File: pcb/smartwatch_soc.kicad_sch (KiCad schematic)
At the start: 51 parts, among them J2 USB_B_Micro, Q1 PN2222A, Q2 PN2222A, Q3 BC338, Q4 BC338, SW1 EN_Switch, SW2 Button, SW3 Button, SW4 Button, SW5 Button, SW6 SW_MEC_5G, SW7 SW_MEC_5G, U1 ESP32-S3-MINI-1U, U2 LSM6DS3, U3 OLED_Display, U4 CP2102N-Axx-xQFN28

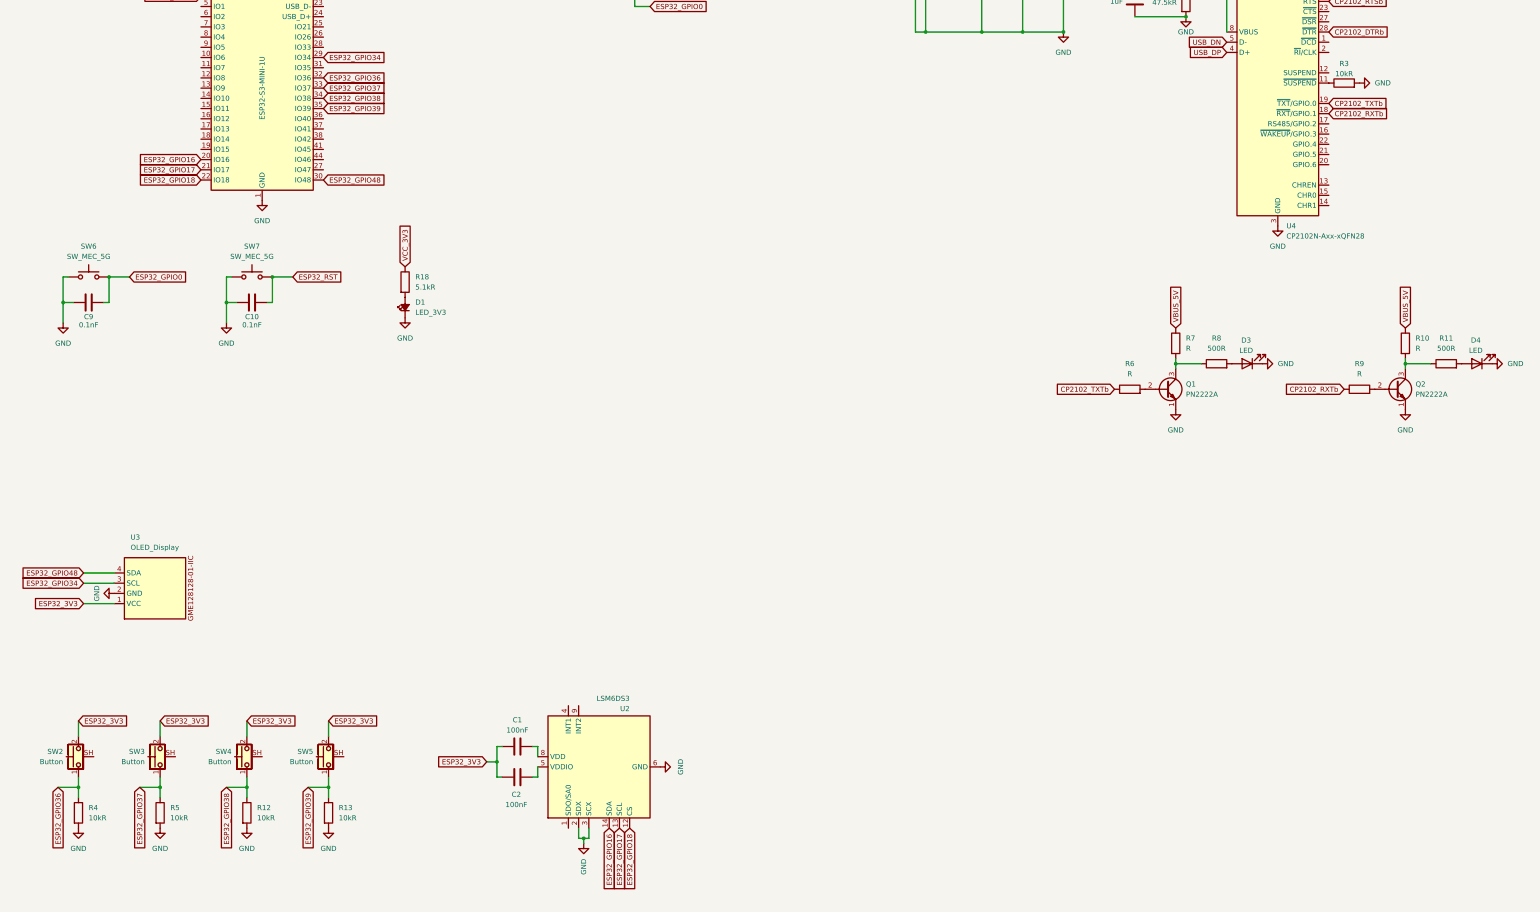
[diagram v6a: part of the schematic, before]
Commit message: fixed resistors for leds and capacitors for accelerometer
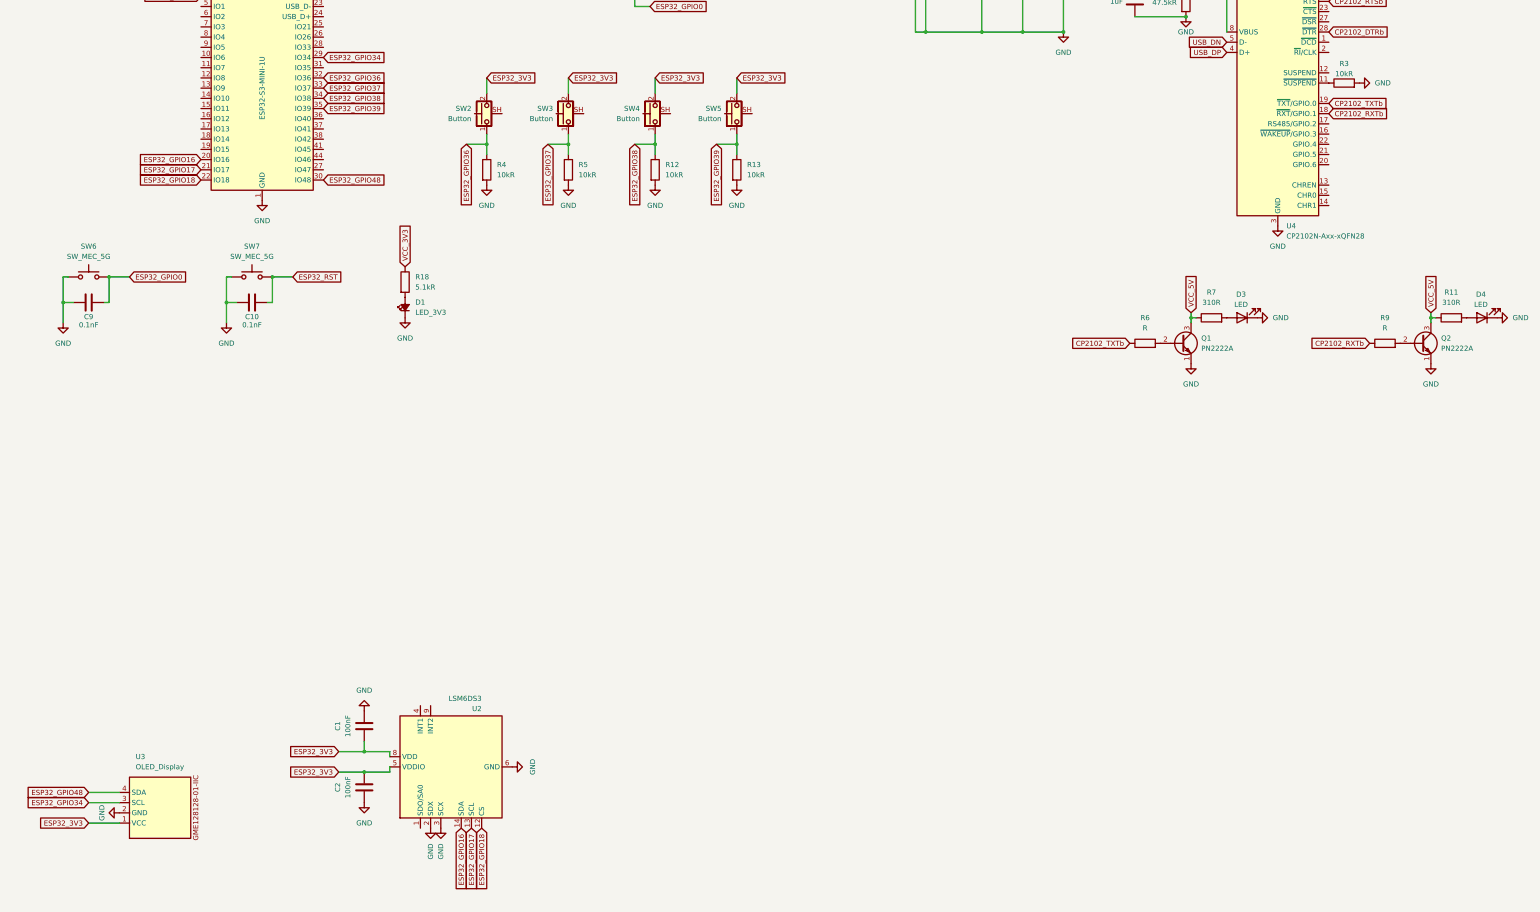
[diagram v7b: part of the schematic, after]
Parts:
- removed R10: R, Resistor_THT:R_Axial_DIN0204_L3.6mm_D1.6mm_P2.54mm_Vertical, symbol Device:R
- removed R8: 500R, Resistor_THT:R_Axial_DIN0204_L3.6mm_D1.6mm_P2.54mm_Vertical, symbol Device:R
- R11: value 500R -> 310R
- R7: value R -> 310R
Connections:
- net VBUS_5V is gone; now on net VCC_5V: R7.1
- net ESP32_3V3: now also C2.2, U2.5 (VDDIO), U2.8 (VDD); no longer C2.1
- net GND: now also C1.2, C2.1
- net VCC_5V: now also Q1.3 (C), Q2.3 (C), R11.1
- net at R7.2: now also D3.2 (A); no longer Q1.3 (C)
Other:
- moved on the sheet: C1, D3, D4, Q1, Q2, R11, R12, R13, R4, R5, R6, R7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

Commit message: use esp32-mini for antenna
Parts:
- removed U1: ESP32-S3-MINI-1U, RF_Module:ESP32-S2-MINI-1U, symbol RF_Module:ESP32-S3-MINI-1U
- added U5: ESP32-S3-MINI-1, RF_Module:ESP32-S2-MINI-1, symbol RF_Module:ESP32-S3-MINI-1
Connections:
- net ESP32_3V3: now also U5.3 (3V3)
- net ESP32_GPIO0: now also U5.4 (IO0)
- net ESP32_GPIO16: now also U5.20 (IO16)
- net ESP32_GPIO17: now also U5.21 (IO17)
- net ESP32_GPIO18: now also U5.22 (IO18)
- net ESP32_GPIO34: now also U5.29 (IO34)
- net ESP32_GPIO36: now also U5.32 (IO36)
- net ESP32_GPIO37: now also U5.33 (IO37)
- net ESP32_GPIO38: now also U5.34 (IO38)
- net ESP32_GPIO39: now also U5.35 (IO39)
- net ESP32_GPIO48: now also U5.30 (IO48)
- net ESP32_RST: now also U5.45 (EN)
- net ESP32_RXD0: now also U5.40 (RXD0)
- net ESP32_TXD0: now also U5.39 (TXD0)
- net GND: now also U5.1 (GND), U5.2 (GND), U5.42 (GND), U5.43 (GND), U5.46 (GND), U5.47 (GND), U5.48 (GND), U5.49 (GND), U5.50 (GND), U5.51 (GND), U5.52 (GND), U5.53 (GND), U5.54 (GND), U5.55 (GND), U5.56 (GND), U5.57 (GND), U5.58 (GND), U5.59 (GND), U5.60 (GND), U5.61 (GND), U5.62 (GND), U5.63 (GND), U5.64 (GND), U5.65 (GND)
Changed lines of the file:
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@@
 	)
 	(symbol
+		(lib_id "RF_Module:ESP32-S3-MINI-1")
+		(at 81.28 74.93 0)
+		(unit 1)
+		(exclude_from_sim no)
+		(in_bom yes)
+		(on_board yes)
+		(dnp no)
+		(property "Reference" "U5"
+			(at 83.4233 41.91 0)
+			(effects
+				(font
+					(size 1.27 1.27)
+				)
+				(justify left)
+			)
+		)
+		(property "Value" "ESP32-S3-MINI-1"
+			(at 81.026 82.296 90)
+			(effects
+				(font
+					(size 1.27 1.27)
+				)
+				(justify left)
+			)
+		)
+		(property "Footprint" "RF_Module:ESP32-S2-MINI-1"
+			(at 96.52 104.14 0)
+			(effects
+				(font
+					(size 1.27 1.27)
+				)
+				(hide yes)
+			)
+		)
+		(property "Datasheet" "https://www.espressif.com/sites/default/files/documentation/esp32-s3-mini-1_mini-1u_datasheet_en.pdf"
+			(at 81.28 34.29 0)
+			(effects
+				(font
+					(size 1.27 1.27)
+				)
+				(hide yes)
+			)
+		)
+		(property "Description" "RF Module, ESP32-S3 SoC, Wi-Fi 802.11b/g/n, Bluetooth, BLE, 32-bit, 3.3V, SMD, onboard antenna"
+			(at 81.28 31.75 0)
+			(effects
+				(font
+					(size 1.27 1.27)
+				)
+				(hide yes)
+			)
+		)
+		(pin "53"
+		)
+		(pin "39"
+		)
+		(pin "56"
+		)
+		(pin "21"
+		)
+		(pin "1"
+		)
+		(pin "37"
+		)
+		(pin "59"
+		)
+		(pin "3"
+		)
+		(pin "15"
+		)
+		(pin "22"
+		)
+		(pin "57"
+		)
+		(pin "61"
+		)
+		(pin "27"
+		)
+		(pin "2"
+		)
+		(pin "65"
+		)
+		(pin "31"
+		)
+		(pin "20"
+		)
+		(pin "47"
+		)
+		(pin "30"
+		)
+		(pin "58"
+		)
+		(pin "60"
+		)
+		(pin "43"
+		)
+		(pin "55"
+		)
+		(pin "35"
+		)
+		(pin "23"
+		)
+		(pin "19"
+		)
+		(pin "52"
+		)
+		(pin "40"
+		)
+		(pin "42"
+		)
+		(pin "11"
+		)
+		(pin "18"
+		)
+		(pin "48"
+		)
+		(pin "63"
+		)
+		(pin "13"
+		)
+		(pin "64"
+		)
+		(pin "8"
+		)
+		(pin "33"
+		)
+		(pin "38"
+		)
+		(pin "44"
+		)
+		(pin "49"
+		)
+		(pin "28"
+		)
+		(pin "25"
+		)
+		(pin "50"
+		)
+		(pin "62"
+		)
+		(pin "41"
+		)
+		(pin "32"
+		)
+		(pin "10"
+		)
+		(pin "54"
+		)
+		(pin "17"
+		)
+		(pin "4"
+		)
+		(pin "6"
+		)
+		(pin "7"
+		)
+		(pin "16"
+		)
+		(pin "45"
+		)
+		(pin "26"
+		)
+		(pin "12"
+		)
+		(pin "24"
+		)
+		(pin "46"
+		)
+		(pin "14"
+		)
+		(pin "9"
+		)
+		(pin "5"
+		)
+		(pin "36"
+		)
+		(pin "51"
+		)
+		(pin "34"
+		)
+		(pin "29"
+		)
+		(instances
+			(project ""
+				(path "/35fbcf8c-23e2-4364-8111-b69121d03e91"
+					(reference "U5")
+					(unit 1)
+				)
+			)
+		)
+	)
+	(symbol
 		(lib_id "Device:C")
 		(at 39.37 36.83 0)
@@
 					(unit 1)
 				)
-			)
-		)
-	)
-	(symbol
-		(lib_id "RF_Module:ESP32-S3-MINI-1U")
-		(at 81.28 74.93 0)
-		(unit 1)
-		(exclude_from_sim no)
-		(in_bom yes)
-		(on_board yes)
-		(dnp no)
-		(property "Reference" "U1"
-			(at 75.184 45.72 0)
-			(effects
-				(font
-					(size 1.27 1.27)
-				)
-				(justify left)
-			)
-		)
-		(property "Value" "ESP32-S3-MINI-1U"
-			(at 81.28 85.344 90)
-			(effects
-				(font
-					(size 1.27 1.27)
-				)
-				(justify left)
-			)
-		)
-		(property "Footprint" "RF_Module:ESP32-S2-MINI-1U"
-			(at 97.79 104.14 0)
-			(effects
-				(font
-					(size 1.27 1.27)
-				)
-				(hide yes)
-			)
-		)
-		(property "Datasheet" "https://www.espressif.com/sites/default/files/documentation/esp32-s3-mini-1_mini-1u_datasheet_en.pdf"
-			(at 81.28 34.29 0)
-			(effects
-				(font
-					(size 1.27 1.27)
-				)
-				(hide yes)
-			)
-		)
-		(property "Description" "RF Module, ESP32-S3 SoC, Wi-Fi 802.11b/g/n, Bluetooth, BLE, 32-bit, 3.3V, SMD, external antenna"
-			(at 81.28 31.75 0)
-			(effects
-				(font
-					(size 1.27 1.27)
-				)
-				(hide yes)
-			)
-		)
-		(pin "36"
-		)
-		(pin "32"
-		)
-		(pin "13"
-		)
-		(pin "27"
-		)
-		(pin "26"
-		)
-		(pin "30"
-		)
-		(pin "56"
-		)
-		(pin "62"
-		)
-		(pin "31"
-		)
-		(pin "28"
-		)
-		(pin "64"
-		)
-		(pin "61"
-		)
-		(pin "39"
-		)
-		(pin "4"
-		)
-		(pin "6"
-		)
-		(pin "58"
-		)
-		(pin "7"
-		)
-		(pin "5"
-		)
-		(pin "33"
-		)
-		(pin "53"
-		)
-		(pin "60"
-		)
-		(pin "24"
-		)
-		(pin "40"
-		)
-		(pin "9"
-		)
-		(pin "8"
-		)
-		(pin "47"
-		)
-		(pin "10"
-		)
-		(pin "46"
-		)
-		(pin "45"
-		)
-		(pin "54"
-		)
-		(pin "43"
-		)
-		(pin "55"
-		)
-		(pin "15"
-		)
-		(pin "41"
-		)
-		(pin "38"
-		)
-		(pin "44"
-		)
-		(pin "52"
-		)
-		(pin "35"
-		)
-		(pin "29"
-		)
-		(pin "50"
-		)
-		(pin "23"
-		)
-		(pin "34"
-		)
-		(pin "42"
-		)
-		(pin "65"
-		)
-		(pin "37"
-		)
-		(pin "51"
-		)
-		(pin "59"
-		)
-		(pin "57"
-		)
-		(pin "20"
-		)
-		(pin "21"
-		)
-		(pin "16"
-		)
-		(pin "14"
-		)
-		(pin "25"
-		)
-		(pin "49"
-		)
-		(pin "1"
-		)
-		(pin "17"
-		)
-		(pin "11"
-		)
-		(pin "63"
-		)
-		(pin "3"
-		)
-		(pin "12"
-		)
-		(pin "22"
-		)
-		(pin "19"
-		)
-		(pin "48"
-		)
-		(pin "2"
-		)
-		(pin "18"
-		)
-		(instances
-			(project ""
-				(path "/35fbcf8c-23e2-4364-8111-b69121d03e91"
-					(reference "U1")
-					(unit 1)
-				)
